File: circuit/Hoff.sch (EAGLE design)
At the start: 25 parts, among them IC1 74595D(ROUND), IC2 24LC256SN

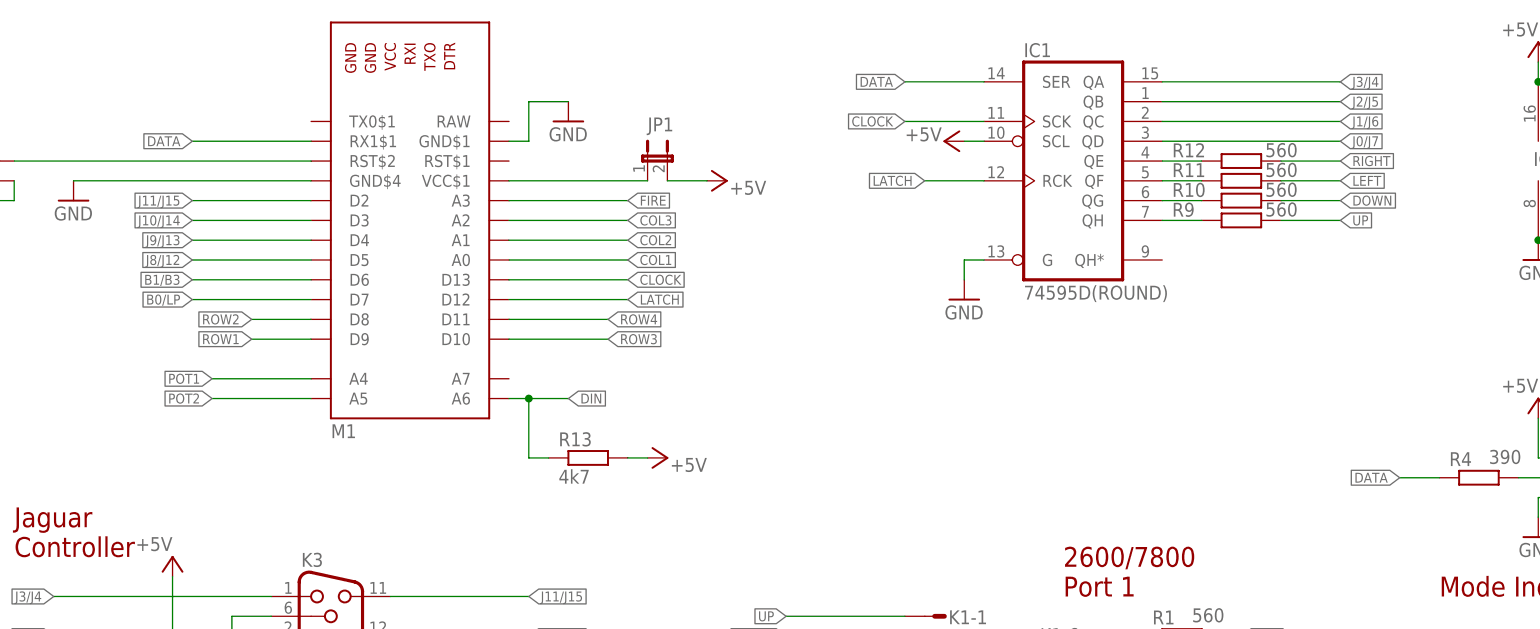
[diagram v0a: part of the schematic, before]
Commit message: Added neopixel to indicate operating mode
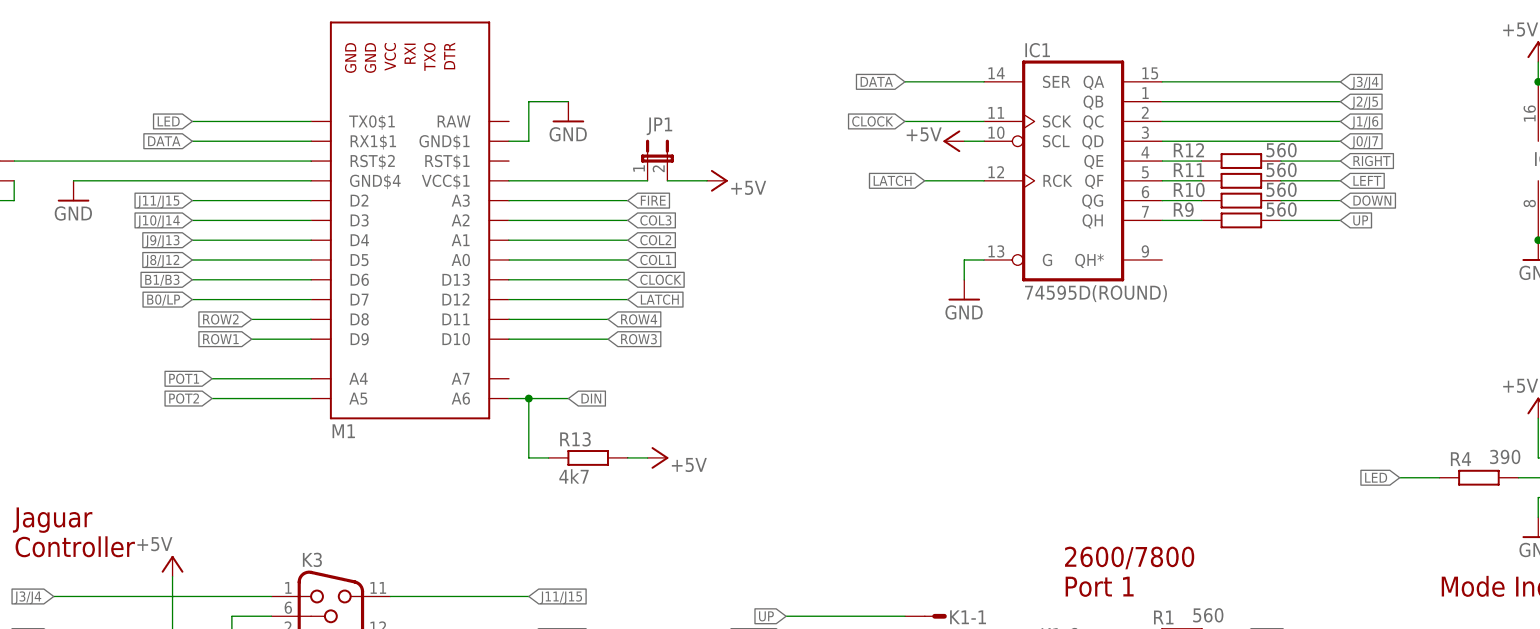
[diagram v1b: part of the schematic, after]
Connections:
- new net LED: M1.TX0$1, R4.1
- net DATA: no longer R4.1
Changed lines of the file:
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@@
-</segment>
-<segment>
-<wire x1="215.9" y1="101.6" x2="210.82" y2="101.6" width="0.1524" layer="91"/>
-<pinref part="R4" gate="G$1" pin="1"/>
-<label x="210.82" y="101.6" size="1.27" layer="95" rot="R180" xref="yes"/>
 </segment>
 <segment>
@@
 </segment>
 </net>
+<net name="LED" class="0">
+<segment>
+<pinref part="M1" gate="G$1" pin="TX0$1"/>
+<wire x1="71.12" y1="147.32" x2="55.88" y2="147.32" width="0.1524" layer="91"/>
+<label x="55.88" y="147.32" size="1.27" layer="95" rot="R180" xref="yes"/>
+</segment>
+<segment>
+<wire x1="215.9" y1="101.6" x2="210.82" y2="101.6" width="0.1524" layer="91"/>
+<pinref part="R4" gate="G$1" pin="1"/>
+<label x="210.82" y="101.6" size="1.27" layer="95" rot="R180" xref="yes"/>
+</segment>
+</net>
